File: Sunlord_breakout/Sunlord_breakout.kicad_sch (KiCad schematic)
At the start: 11 parts, among them J1 AH, J2 AL, J3 BH, J4 BL, J5 CH, J6 CL, J7 DH, J8 DL, T1 Transformer_1P_1S

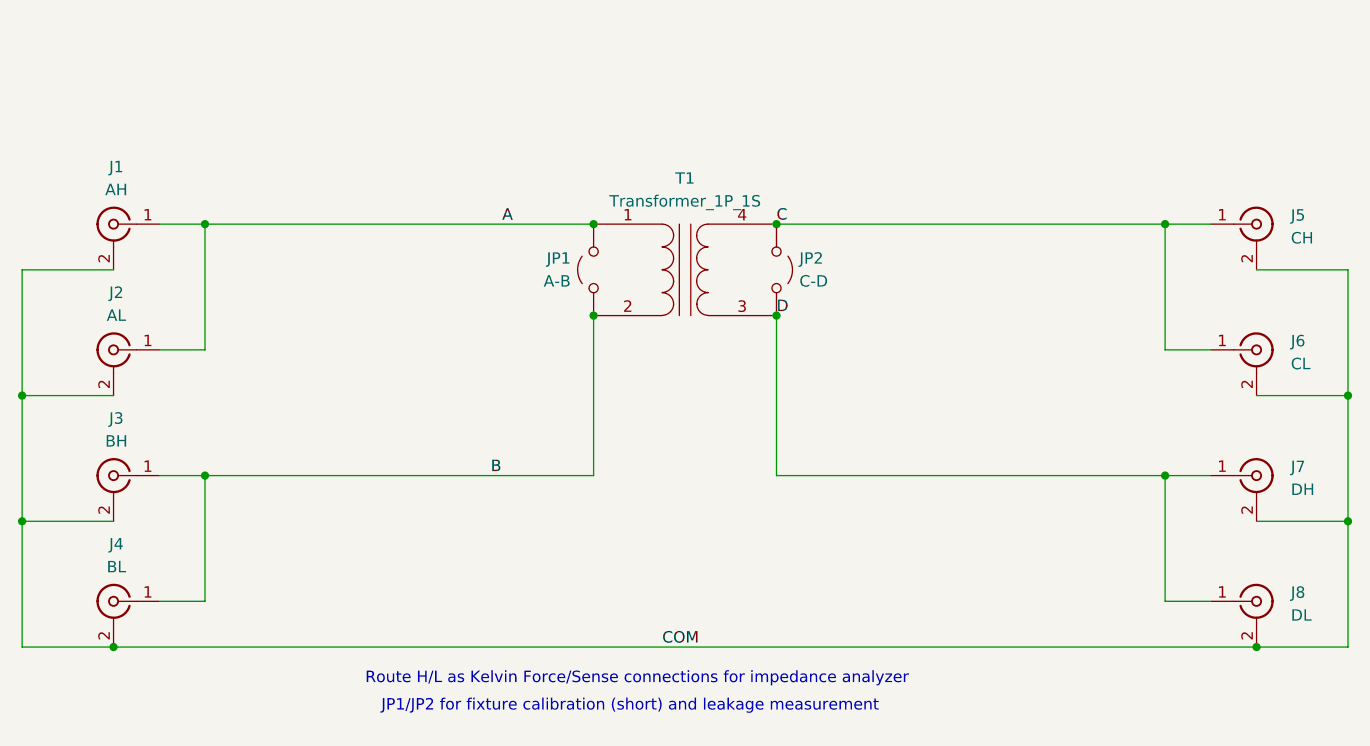
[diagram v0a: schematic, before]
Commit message: added sunlord breakout
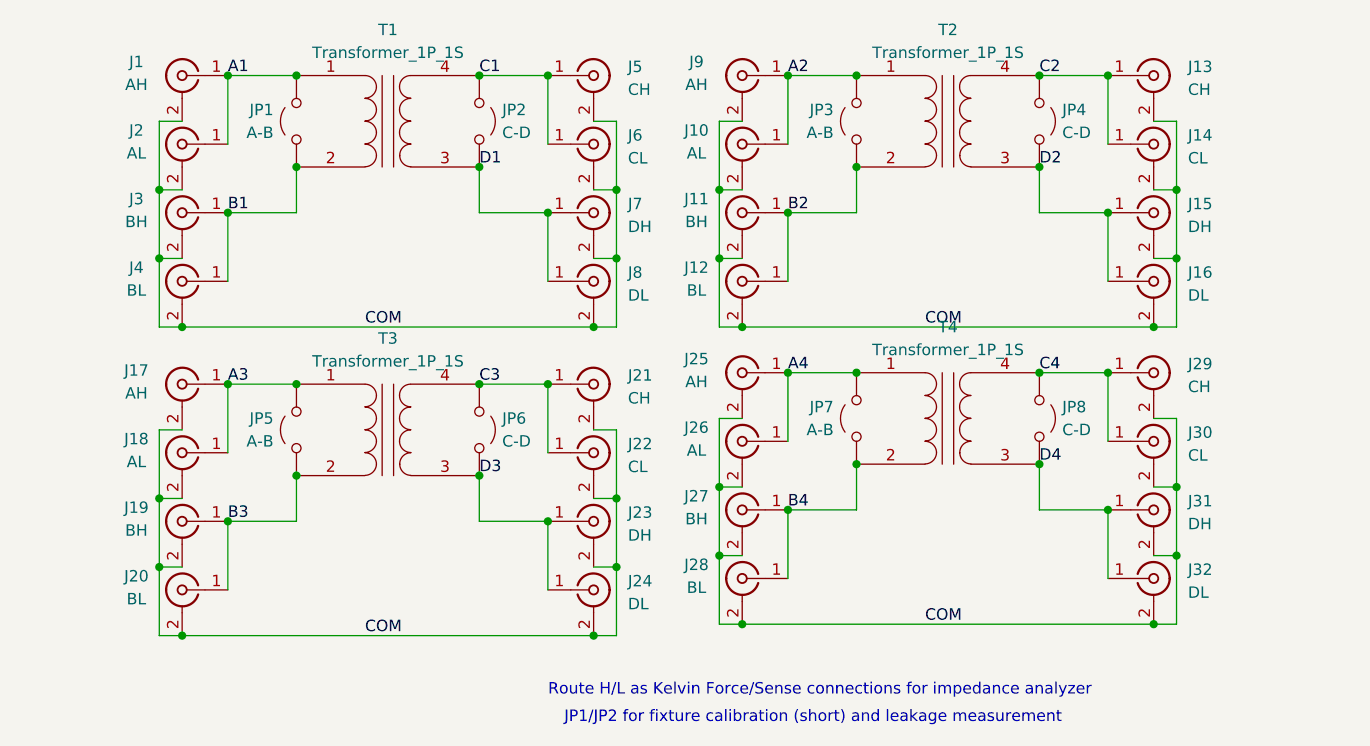
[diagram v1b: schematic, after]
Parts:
- added J10, J18, J26: AL, Connector_Coaxial:SMA_Samtec_SMA-J-P-H-ST-EM1_EdgeMount, symbol Connector:Conn_Coaxial
- added J11, J19, J27: BH, Connector_Coaxial:SMA_Samtec_SMA-J-P-H-ST-EM1_EdgeMount, symbol Connector:Conn_Coaxial
- added J12, J20, J28: BL, Connector_Coaxial:SMA_Samtec_SMA-J-P-H-ST-EM1_EdgeMount, symbol Connector:Conn_Coaxial
- added J13, J21, J29: CH, Connector_Coaxial:SMA_Samtec_SMA-J-P-H-ST-EM1_EdgeMount, symbol Connector:Conn_Coaxial
- added J14, J22, J30: CL, Connector_Coaxial:SMA_Samtec_SMA-J-P-H-ST-EM1_EdgeMount, symbol Connector:Conn_Coaxial
- added J15, J23, J31: DH, Connector_Coaxial:SMA_Samtec_SMA-J-P-H-ST-EM1_EdgeMount, symbol Connector:Conn_Coaxial
- added J16, J24, J32: DL, Connector_Coaxial:SMA_Samtec_SMA-J-P-H-ST-EM1_EdgeMount, symbol Connector:Conn_Coaxial
- added J17, J25, J9: AH, Connector_Coaxial:SMA_Samtec_SMA-J-P-H-ST-EM1_EdgeMount, symbol Connector:Conn_Coaxial
- added JP3, JP5, JP7: A-B, Jumper:SolderJumper-2_P1.3mm_Open_RoundedPad1.0x1.5mm, symbol Jumper:Jumper_2_Open
- added JP4, JP6, JP8: C-D, Jumper:SolderJumper-2_P1.3mm_Open_RoundedPad1.0x1.5mm, symbol Jumper:Jumper_2_Open
- added T2, T3, T4: Transformer_1P_1S, footprints:AW2222_Sunlord_µXFMR, symbol Device:Transformer_1P_1S
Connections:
- net COM: now also J10.2 (Ext), J11.2 (Ext), J12.2 (Ext), J13.2 (Ext), J14.2 (Ext), J15.2 (Ext), J16.2 (Ext), J17.2 (Ext), J18.2 (Ext), J19.2 (Ext), J20.2 (Ext), J21.2 (Ext), J22.2 (Ext), J23.2 (Ext), J24.2 (Ext), J25.2 (Ext), J26.2 (Ext), J27.2 (Ext), J28.2 (Ext), J29.2 (Ext), J30.2 (Ext), J31.2 (Ext), J32.2 (Ext), J9.2 (Ext)
- net A renamed A1
- net B renamed B1
- net C renamed C1
- net D renamed D1
- new net A2: J10.1 (In), J9.1 (In), JP3.2 (B), T2.1 (AA)
- new net A3: J17.1 (In), J18.1 (In), JP5.2 (B), T3.1 (AA)
- new net A4: J25.1 (In), J26.1 (In), JP7.2 (B), T4.1 (AA)
- new net B2: J11.1 (In), J12.1 (In), JP3.1 (A), T2.2 (AB)
- new net B3: J19.1 (In), J20.1 (In), JP5.1 (A), T3.2 (AB)
- new net B4: J27.1 (In), J28.1 (In), JP7.1 (A), T4.2 (AB)
- new net C2: J13.1 (In), J14.1 (In), JP4.1 (A), T2.4 (SB)
- new net C3: J21.1 (In), J22.1 (In), JP6.1 (A), T3.4 (SB)
- new net C4: J29.1 (In), J30.1 (In), JP8.1 (A), T4.4 (SB)
- new net D2: J15.1 (In), J16.1 (In), JP4.2 (B), T2.3 (SA)
- new net D3: J23.1 (In), J24.1 (In), JP6.2 (B), T3.3 (SA)
- new net D4: J31.1 (In), J32.1 (In), JP8.2 (B), T4.3 (SA)
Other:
- moved on the sheet: J1, J2, J3, J4, J5, J6, J7, J8, JP1, JP2, T1
